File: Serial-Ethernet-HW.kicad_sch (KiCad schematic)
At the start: 0 parts

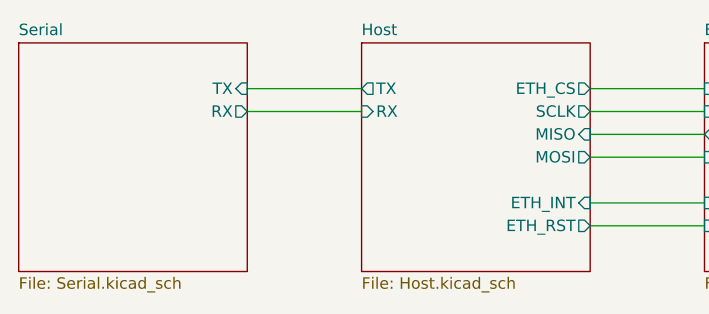
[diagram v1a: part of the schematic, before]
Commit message: Add in RS232
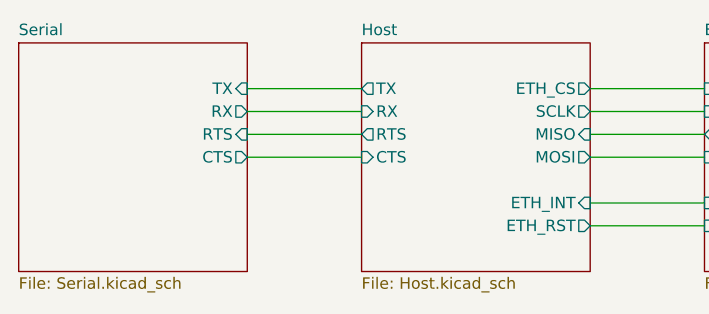
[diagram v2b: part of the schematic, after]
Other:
- sheet Host ports: added CTS, RTS; removed none
- sheet Serial ports: added CTS, RTS; removed none
- company: TL Embedded Ltd -> TL Embedded
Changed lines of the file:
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@@
 	(title_block
 		(title "Serial-Ethernet")
-		(date "2025-09-13")
-		(rev "v1.0b")
-		(company "TL Embedded Ltd")
+		(date "2026-07-23")
+		(rev "v1.1")
+		(company "TL Embedded")
 	)
 	(wire
@@
 		(pts
 			(xy 114.3 43.18) (xy 127 43.18)
+		)
+		(stroke
+			(width 0)
+			(type default)
+		)
+	)
+	(wire
+		(pts
+			(xy 76.2 50.8) (xy 88.9 50.8)
+		)
+		(stroke
+			(width 0)
+			(type default)
+		)
+	)
+	(wire
+		(pts
+			(xy 76.2 48.26) (xy 88.9 48.26)
 		)
 		(stroke
@@
 			)
 		)
+		(pin "CTS" output
+			(at 76.2 50.8 0)
+			(effects
+				(font
+					(size 1.27 1.27)
+				)
+				(justify right)
+			)
+		)
+		(pin "RTS" input
+			(at 76.2 48.26 0)
+			(effects
+				(font
+					(size 1.27 1.27)
+				)
+				(justify right)
+			)
+		)
 		(instances
 			(project "Serial-Ethernet-HW"
@@
 			(effects
 				(font
+					(size 1.27 1.27)
+				)
+				(justify left)
+			)
+		)
+		(pin "CTS" input
+			(at 88.9 50.8 180)
+			(effects
+				(font
+					(size 1.27 1.27)
+				)
+				(justify left)
+			)
+		)
+		(pin "RTS" output
+			(at 88.9 48.26 180)
+			(effects
+				(font

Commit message: PCB Layout
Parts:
- added N2, N3, N4: ToolingHole, N_NonPart:ToolingHole_1mm, symbol N_NonPart:ToolingHole_1mm
- added N5: QR 5mm, N_NonPart:QR_5mm_JLC, symbol N_NonPart:QR_5mm_JLC
